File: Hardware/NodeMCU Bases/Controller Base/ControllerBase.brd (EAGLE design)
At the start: 48.3 x 25.4 mm, 8 parts

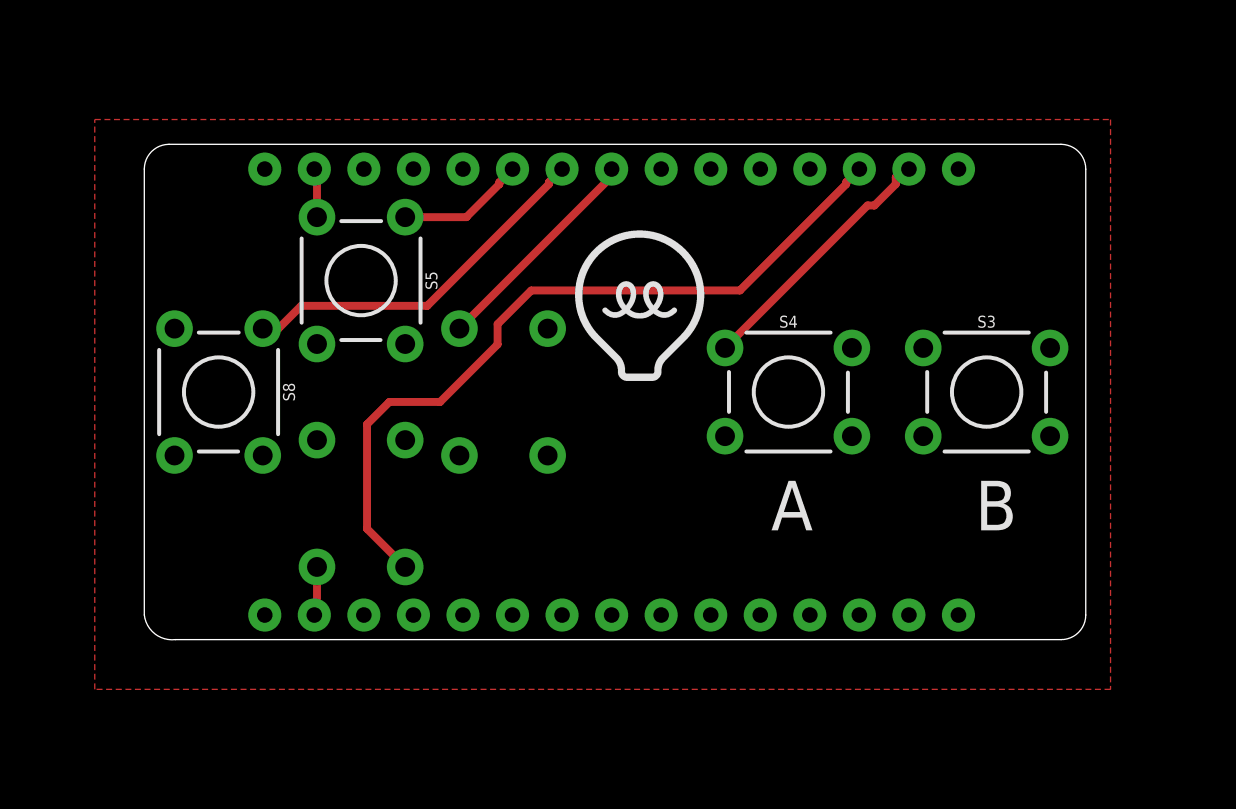
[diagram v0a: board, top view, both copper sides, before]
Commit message: HEEP-949 updated from legacy cam for current Eagle Compatability. Also removed bName layer from bottom Silk
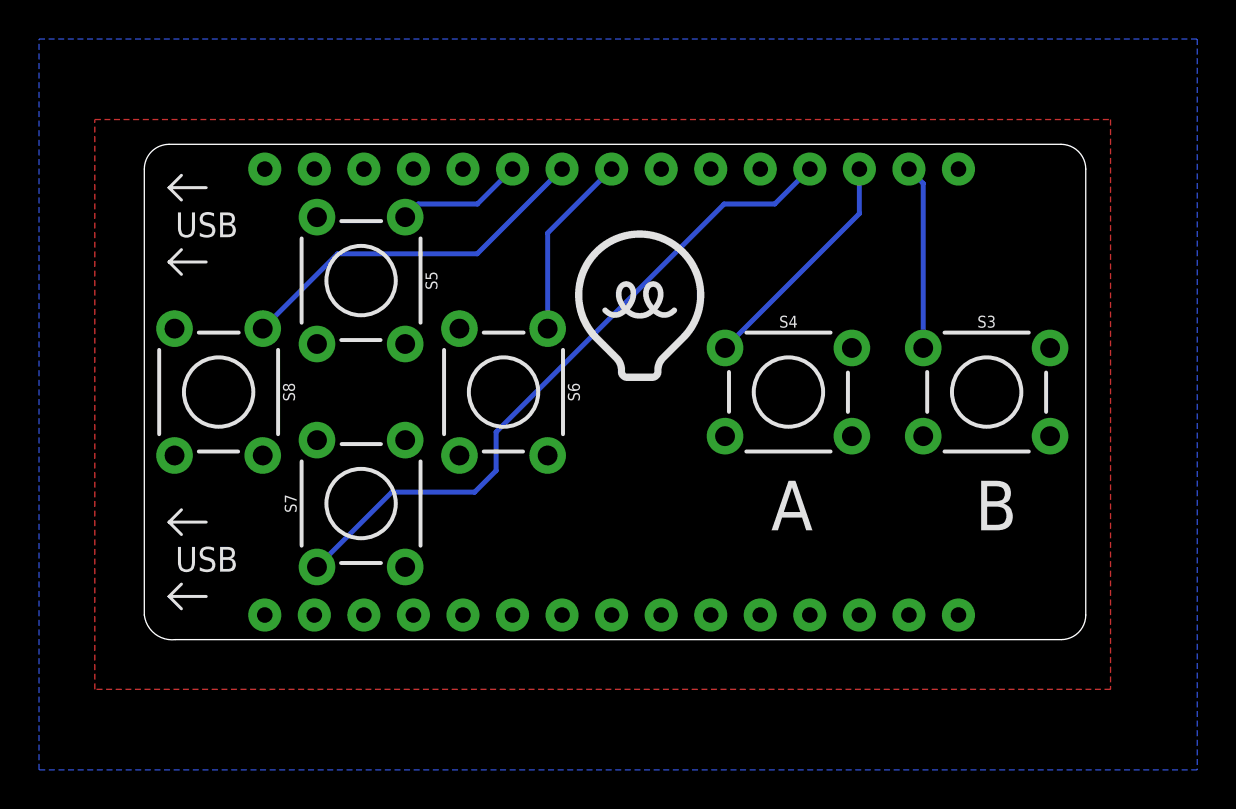
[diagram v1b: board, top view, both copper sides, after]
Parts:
- flipped S6 to the top
- flipped S7 to the top
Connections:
- removed net 0: S3.1, U$1.D0
- removed net 4: U$1.D4
- removed net 8: U$1.D8
- new net 3: S7.1, U$1.D3
- net 1: now also S3.1; no longer S4.1
- net 2: now also S4.1; no longer S7.1
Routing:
- net 3: track 0.00 -> 34.9 mm
- net 2: track 39.4 -> 12.0 mm
- net GND: track 5.23 -> 0.00 mm
- net 1: track 13.4 -> 9.47 mm
- net 5: track 11.4 -> 9.54 mm
- added copper zone on layer 16, net GND
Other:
- board text added: "USB"
